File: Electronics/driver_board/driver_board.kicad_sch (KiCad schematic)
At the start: 12 parts, among them J1 Conn_ST_STDC14, SW1 TL3305, U1 STM32G491CCT6

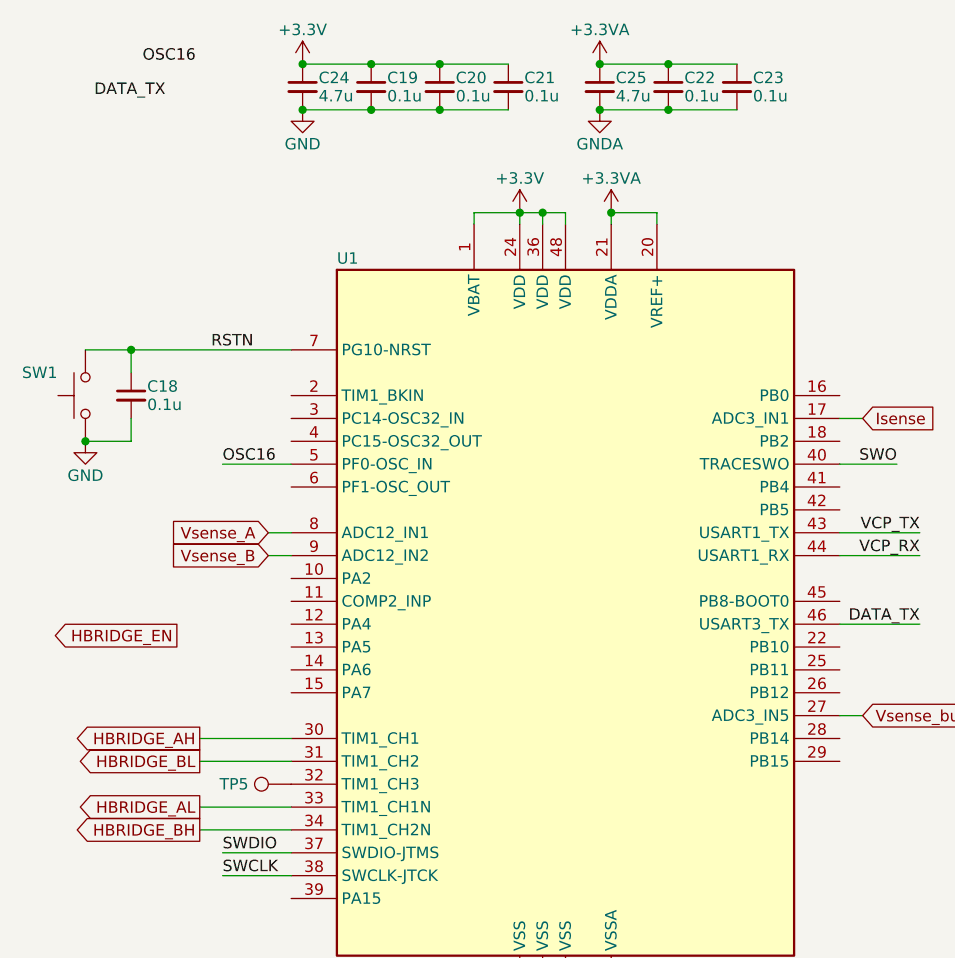
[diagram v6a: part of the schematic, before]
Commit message: Added TVS diodes, bulk capacitors
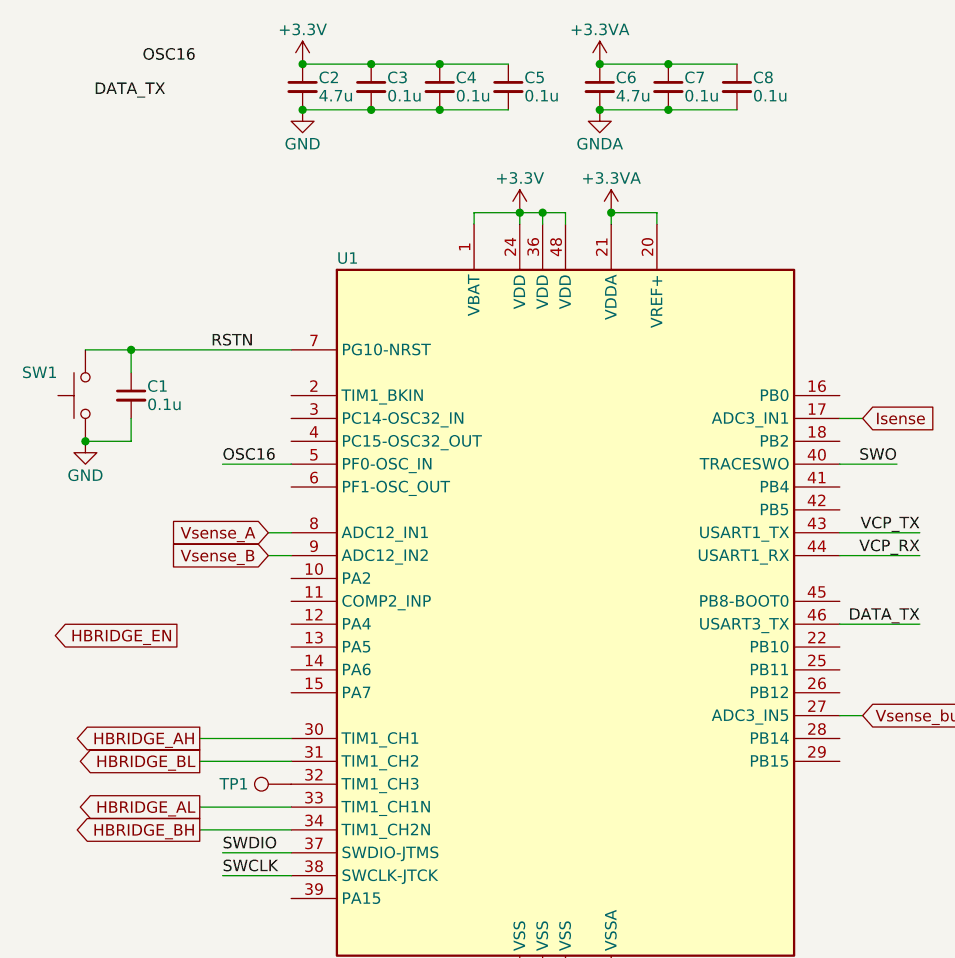
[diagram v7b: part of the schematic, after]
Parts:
- C1: renamed from C18; footprint (none) -> Capacitor_SMD:C_0402_1005Metric
- C2: renamed from C24; footprint (none) -> Capacitor_SMD:C_0603_1608Metric
- C3: renamed from C19; footprint (none) -> Capacitor_SMD:C_0402_1005Metric
- C4: renamed from C20; footprint (none) -> Capacitor_SMD:C_0402_1005Metric
- C5: renamed from C21; footprint (none) -> Capacitor_SMD:C_0402_1005Metric
- C6: renamed from C25; footprint (none) -> Capacitor_SMD:C_0603_1608Metric
- C7: renamed from C22; footprint (none) -> Capacitor_SMD:C_0402_1005Metric
- C8: renamed from C23; footprint (none) -> Capacitor_SMD:C_0402_1005Metric
- renumbered TP5 to TP1
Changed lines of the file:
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@@
 		(on_board yes)
 		(dnp no)
-		(property "Reference" "C23"
+		(property "Reference" "C8"
 			(at 98.298 29.464 0)
 			(effects
@@
 			)
 		)
-		(property "Footprint" ""
+		(property "Footprint" "Capacitor_SMD:C_0402_1005Metric"
 			(at 96.52 30.48 0)
 			(effects
@@
 			(project "driver_board"
 				(path "/90d9ae7d-4001-450f-acdb-4ca976b51116"
-					(reference "C23")
+					(reference "C8")
 					(unit 1)
 				)
@@
 		(on_board yes)
 		(dnp no)
-		(property "Reference" "#PWR04"
+		(property "Reference" "#PWR07"
 			(at 74.93 139.7 0)
 			(effects
@@
 			(project ""
 				(path "/90d9ae7d-4001-450f-acdb-4ca976b51116"
-					(reference "#PWR04")
+					(reference "#PWR07")
 					(unit 1)
 				)
@@
 		(on_board yes)
 		(dnp no)
-		(property "Reference" "#PWR051"
+		(property "Reference" "#PWR04"
 			(at 48.26 31.75 0)
 			(effects
@@
 			(project "driver_board"
 				(path "/90d9ae7d-4001-450f-acdb-4ca976b51116"
-					(reference "#PWR051")
+					(reference "#PWR04")
 					(unit 1)
 				)
@@
 		(on_board yes)
 		(dnp no)
-		(property "Reference" "#PWR050"
+		(property "Reference" "#PWR01"
 			(at 24.13 76.2 0)
 			(effects
@@
 			(project "driver_board"
 				(path "/90d9ae7d-4001-450f-acdb-4ca976b51116"
-					(reference "#PWR050")
+					(reference "#PWR01")
 					(unit 1)
 				)
@@
 		(on_board yes)
 		(dnp no)
-		(property "Reference" "C24"
+		(property "Reference" "C2"
 			(at 50.038 29.464 0)
 			(effects
@@
 			)
 		)
-		(property "Footprint" ""
+		(property "Footprint" "Capacitor_SMD:C_0603_1608Metric"
 			(at 48.26 30.48 0)
 			(effects
@@
 			(project "driver_board"
 				(path "/90d9ae7d-4001-450f-acdb-4ca976b51116"
-					(reference "C24")
+					(reference "C2")
 					(unit 1)
 				)
@@
 		(on_board yes)
 		(dnp no)
-		(property "Reference" "#PWR054"
+		(property "Reference" "#PWR09"
 			(at 81.28 39.37 0)
 			(effects
@@
 			(project "driver_board"
 				(path "/90d9ae7d-4001-450f-acdb-4ca976b51116"
-					(reference "#PWR054")
+					(reference "#PWR09")
 					(unit 1)
 				)
@@
 		(on_board yes)
 		(dnp no)
-		(property "Reference" "#PWR02"
+		(property "Reference" "#PWR03"
 			(at 43.18 186.69 0)
 			(effects
@@
 			(project "driver_board"
 				(path "/90d9ae7d-4001-450f-acdb-4ca976b51116"
-					(reference "#PWR02")
+					(reference "#PWR03")
 					(unit 1)
 				)
@@
 		(on_board yes)
 		(dnp no)
-		(property "Reference" "C19"
+		(property "Reference" "C3"
 			(at 57.658 29.464 0)
 			(effects
@@
 			)
 		)
-		(property "Footprint" ""
+		(property "Footprint" "Capacitor_SMD:C_0402_1005Metric"
 			(at 55.88 30.48 0)
 			(effects
@@
 			(project "driver_board"
 				(path "/90d9ae7d-4001-450f-acdb-4ca976b51116"
-					(reference "C19")
+					(reference "C3")
 					(unit 1)
 				)
@@
 		(on_board yes)
 		(dnp no)
-		(property "Reference" "#PWR053"
+		(property "Reference" "#PWR05"
 			(at 48.26 39.37 0)
 			(effects
@@
 			(project "driver_board"
 				(path "/90d9ae7d-4001-450f-acdb-4ca976b51116"
-					(reference "#PWR053")
+					(reference "#PWR05")
 					(unit 1)
 				)
@@
 		(on_board yes)
 		(dnp no)
-		(property "Reference" "C22"
+		(property "Reference" "C7"
 			(at 90.678 29.464 0)
 			(effects
@@
 			)
 		)
-		(property "Footprint" ""
+		(property "Footprint" "Capacitor_SMD:C_0402_1005Metric"
 			(at 88.9 30.48 0)
 			(effects
@@
 			(project "driver_board"
 				(path "/90d9ae7d-4001-450f-acdb-4ca976b51116"
-					(reference "C22")
+					(reference "C7")
 					(unit 1)
 				)
@@
 		(on_board yes)
 		(dnp no)
-		(property "Reference" "#PWR052"
+		(property "Reference" "#PWR08"
 			(at 81.28 31.75 0)
 			(effects
@@
 			(project "driver_board"
 				(path "/90d9ae7d-4001-450f-acdb-4ca976b51116"
-					(reference "#PWR052")
+					(reference "#PWR08")
 					(unit 1)
 				)
@@
 		(on_board yes)
 		(dnp no)
-		(property "Reference" "#PWR03"
+		(property "Reference" "#PWR06"
 			(at 72.39 48.26 0)
 			(effects
@@
 			(project ""
 				(path "/90d9ae7d-4001-450f-acdb-4ca976b51116"
-					(reference "#PWR03")
+					(reference "#PWR06")
 					(unit 1)
 				)
@@
 		(on_board yes)
 		(dnp no)
-		(property "Reference" "#PWR05"
+		(property "Reference" "#PWR010"
 			(at 82.55 48.26 0)
 			(effects
@@
 			(project ""
 				(path "/90d9ae7d-4001-450f-acdb-4ca976b51116"
-					(reference "#PWR05")
+					(reference "#PWR010")
 					(unit 1)
 				)
@@
 		(on_board yes)
 		(dnp no)
-		(property "Reference" "C21"
+		(property "Reference" "C5"
 			(at 72.898 29.464 0)
 			(effects
@@
 			)
 		)
-		(property "Footprint" ""
+		(property "Footprint" "Capacitor_SMD:C_0402_1005Metric"
 			(at 71.12 30.48 0)
 			(effects
@@
 			(project "driver_board"
 				(path "/90d9ae7d-4001-450f-acdb-4ca976b51116"
-					(reference "C21")
+					(reference "C5")
 					(unit 1)
 				)
@@
 		(on_board yes)
 		(dnp no)
-		(property "Reference" "C20"
+		(property "Reference" "C4"
 			(at 65.278 29.464 0)
 			(effects
@@
 			)
 		)
-		(property "Footprint" ""
+		(property "Footprint" "Capacitor_SMD:C_0402_1005Metric"
 			(at 63.5 30.48 0)
 			(effects
@@
 			(project "driver_board"
 				(path "/90d9ae7d-4001-450f-acdb-4ca976b51116"
-					(reference "C20")
+					(reference "C4")
 					(unit 1)
 				)
@@
 		(on_board yes)
 		(dnp no)
-		(property "Reference" "C25"
+		(property "Reference" "C6"
 			(at 83.058 29.464 0)
 			(effects
@@
 			)
 		)
-		(property "Footprint" ""
+		(property "Footprint" "Capacitor_SMD:C_0603_1608Metric"
 			(at 81.28 30.48 0)
 			(effects
@@
 			(project "driver_board"
 				(path "/90d9ae7d-4001-450f-acdb-4ca976b51116"
-					(reference "C25")
+					(reference "C6")
 					(unit 1)
 				)
@@
 		(on_board yes)
 		(dnp no)
-		(property "Reference" "TP5"
+		(property "Reference" "TP1"
 			(at 40.64 107.95 90)
 			(effects
@@
 			(project "driver_board"
 				(path "/90d9ae7d-4001-450f-acdb-4ca976b51116"
-					(reference "TP5")
+					(reference "TP1")
 					(unit 1)
 				)
@@
 		(on_board yes)
 		(dnp no)
-		(property "Reference" "#PWR06"
+		(property "Reference" "#PWR011"
 			(at 82.55 139.7 0)
 			(effects
@@
 			(project ""
 				(path "/90d9ae7d-4001-450f-acdb-4ca976b51116"
-					(reference "#PWR06")
+					(reference "#PWR011")
 					(unit 1)
 				)
@@
 		(on_board yes)
 		(dnp no)
-		(property "Reference" "#PWR01"
+		(property "Reference" "#PWR02"
 			(at 43.18 147.32 0)
 			(effects
@@
 			(project "driver_board"
 				(path "/90d9ae7d-4001-450f-acdb-4ca976b51116"
-					(reference "#PWR01")
+					(reference "#PWR02")
 					(unit 1)
 				)
@@
 		(on_board yes)
 		(dnp no)
-		(property "Reference" "C18"
+		(property "Reference" "C1"
 			(at 30.988 63.754 0)
 			(effects
@@
 			)
 		)
-		(property "Footprint" ""
+		(property "Footprint" "Capacitor_SMD:C_0402_1005Metric"
 			(at 29.21 64.77 0)
 			(effects
@@
 			(project "driver_board"
 				(path "/90d9ae7d-4001-450f-acdb-4ca976b51116"
-					(reference "C18")
-					(unit 1)
-				)
+					(reference "C1")
+					(unit 1)
+				)
